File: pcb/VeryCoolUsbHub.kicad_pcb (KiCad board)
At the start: 4 copper layers, 75 x 54.5 mm, 69 parts, among them U1 HD3SS3220RNHR, U2 HD3SS3220RNHR, X1 X322525MSB4SI, X2 X322525MSB4SI

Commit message: fixed signal intergrity stuff
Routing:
- net VBUS: track 201.0 -> 185.4 mm
- net GND: vias 30 -> 35

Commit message: update pcb and changed production file to newest
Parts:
- moved X2 6.39 mm to (193.7, 67.2), turned to 180 degrees
- moved C18 3.04 mm to (193.1, 64.4), turned to 180 degrees
- moved G*** 2.75 mm to (188.1, 75.4)
- moved C25 1.90 mm to (197.1, 67.2), turned to -90 degrees
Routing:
- net VBUS: track 185.4 -> 168.7 mm
- net Net-(USB_CONTROLLER1-X2): track 6.85 -> 17.8 mm
- net Net-(USB_CONTROLLER1-X1): track 6.96 -> 12.6 mm
- net GND: track 122.1 -> 120.7 mm

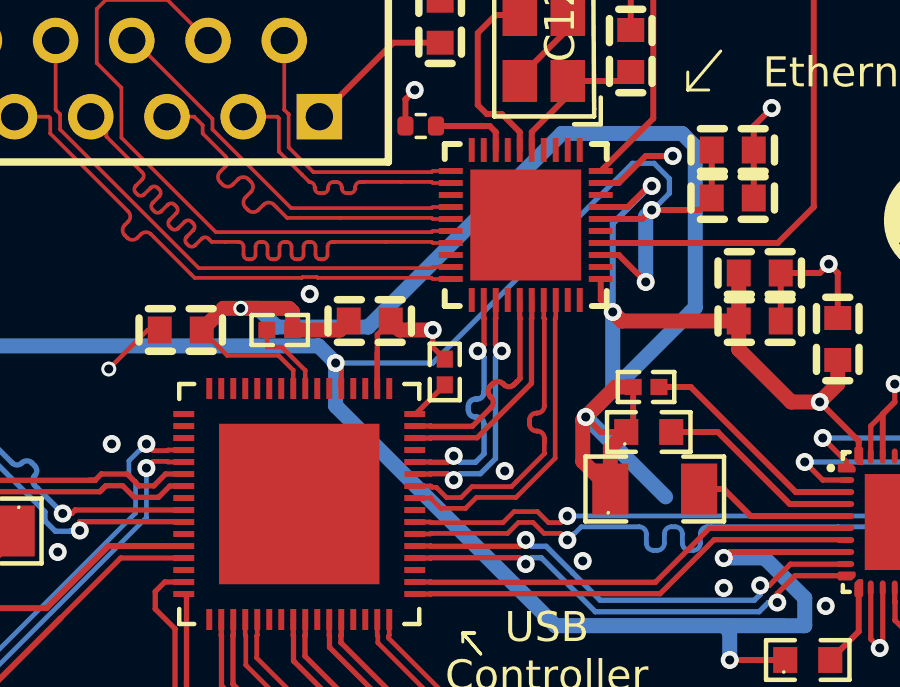
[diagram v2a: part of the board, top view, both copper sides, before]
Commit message: fixed small error in pcb
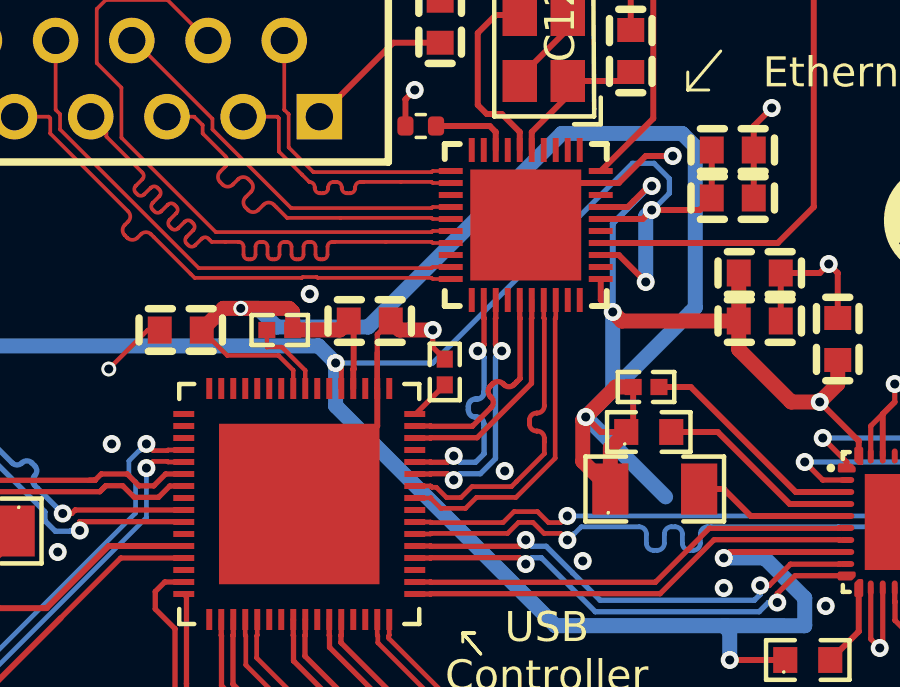
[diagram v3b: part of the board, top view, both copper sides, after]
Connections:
- ETHERNET_CONTROLLER1 pad 41: unconnected-(ETHERNET_CONTROLLER1-EP-Pad41) -> GND
- USB_CONTROLLER1 pad 65: unconnected-(USB_CONTROLLER1-EP-Pad65) -> GND
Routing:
- net GND: track 120.7 -> 128.7 mm
- net VBUS: track 168.7 -> 171.0 mm
